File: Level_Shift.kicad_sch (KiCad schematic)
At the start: 22 parts, among them U23 74AVC4T245, U25 74AVC4T245, U26 74LVC8T245, U27 74LVC8T245

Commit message: Revision based on pre-production
-Added pull-down on the OE for the Digital output buffers
- increase board edge (was 0.3mm, but via and traces are 0.5mm away now)
- move power vias away from board edge
- Increase power via size from 0.6mm/0.3mm to 0.8mm/0.4mm in a couple of places
- Naming of level shifter output enable changed to make function clear throughout the design.
- Revised SMPS layout slightly to better use the space.
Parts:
- added R42, R43: 4.75k, Resistor_SMD:R_0402_1005Metric, symbol Device:R_Small_US
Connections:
- net GND: now also R42.1, R43.1
- net OE_Digital_Outputs_A: now also R43.2
- net OE_Digital_Outputs_B: now also R42.2
- net OE_Faults_0 renamed Cleaner_LevelShift_~{OE}_0
- net OE_Faults_1 renamed Cleaner_LevelShift_~{OE}_1
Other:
- moved on the sheet: R96, R97

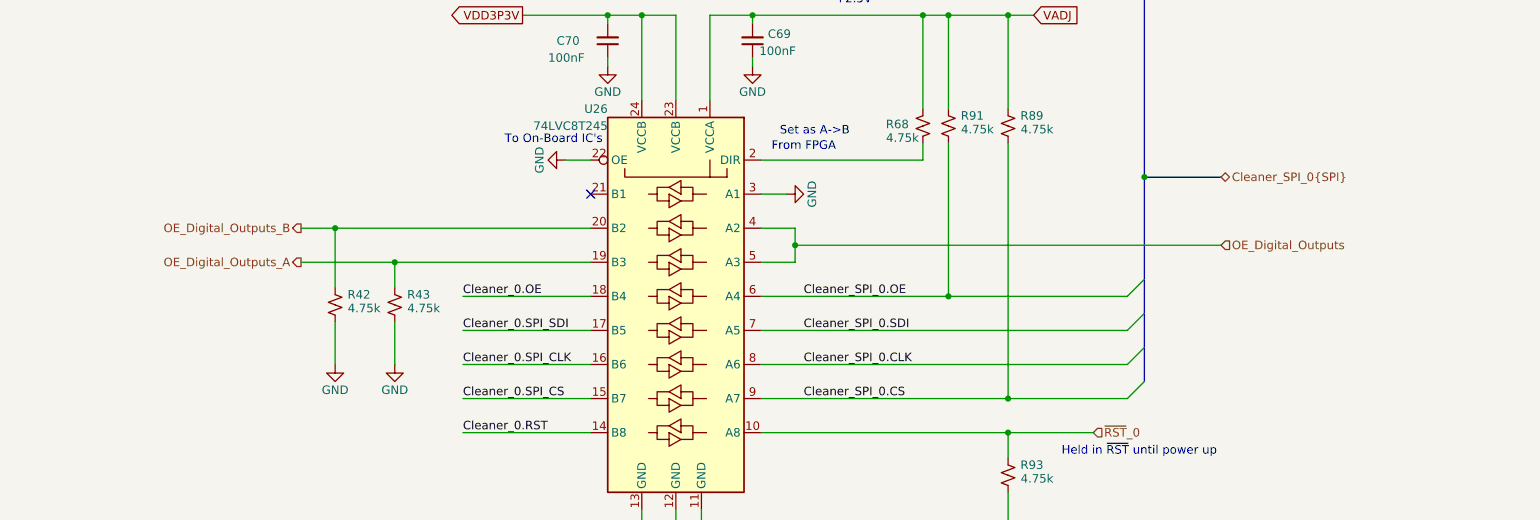
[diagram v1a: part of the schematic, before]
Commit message: Updates from Pre-production boards
- removed ground from mounting holes and added no-pop 0805 resistors to optionally ground the mounting holes.
- Adjusted placement of some test points.
- Made the test point loops non-populated parts, the pads will remain.
- Added silkscreen labels to the test points.
- Fixed pulldown resistor added in prevoius commit.
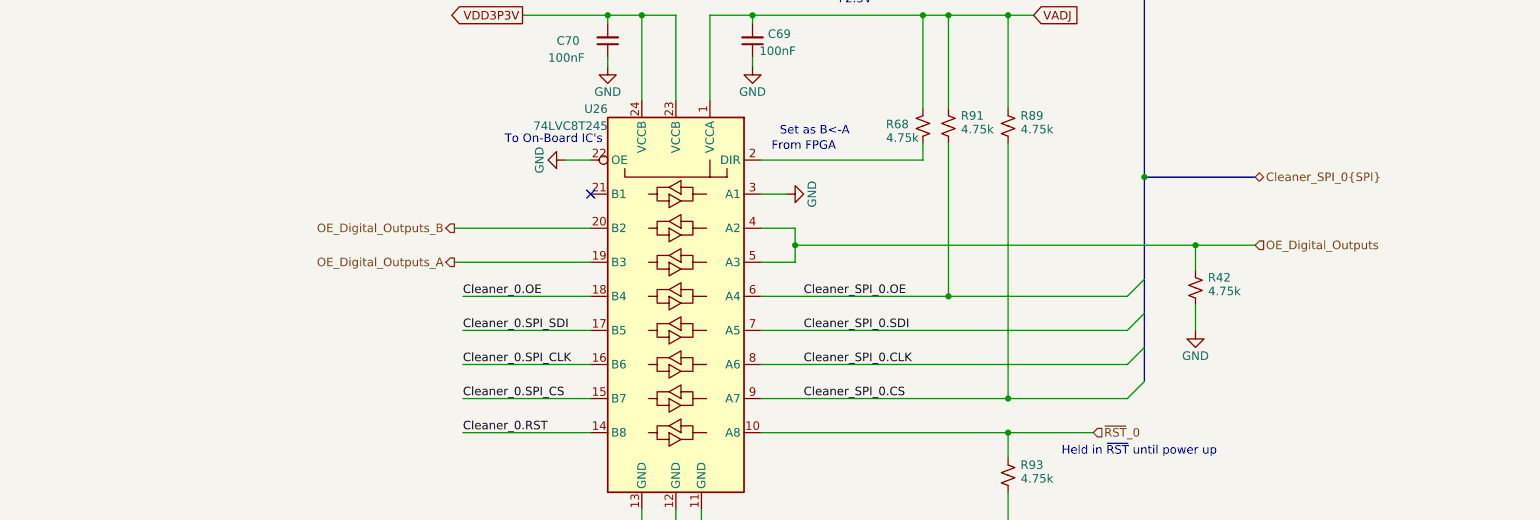
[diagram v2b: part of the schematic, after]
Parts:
- removed R43: 4.75k, Resistor_SMD:R_0402_1005Metric, symbol Device:R_Small_US
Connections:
- net OE_Digital_Outputs: now also R42.2
- net OE_Digital_Outputs_B: no longer R42.2
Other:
- note added: "Set as B<-A"
- moved on the sheet: R42
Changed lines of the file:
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@@
 		)
 	)
-	(text "Set as A->B"
+	(text "Set as B<-A"
 		(exclude_from_sim no)
 		(at 154.178 129.794 0)
@@
 	)
 	(junction
-		(at 77.47 143.51)
-		(diameter 0)
-		(color 0 0 0 0)
-	)
-	(junction
 		(at 297.18 99.06)
 		(diameter 0)
@@
 	)
 	(junction
+		(at 205.74 146.05)
+		(diameter 0)
+		(color 0 0 0 0)
+	)
+	(junction
 		(at 177.8 173.99)
 		(diameter 0)
@@
 	)
 	(junction
-		(at 86.36 148.59)
-		(diameter 0)
-		(color 0 0 0 0)
-	)
-	(junction
 		(at 363.22 134.62)
 		(diameter 0)
@@
 	(wire
 		(pts
-			(xy 86.36 148.59) (xy 86.36 152.4)
-		)
-		(stroke
-			(width 0)
-			(type default)
-		)
-	)
-	(wire
-		(pts
 			(xy 165.1 133.35) (xy 165.1 130.81)
 		)
@@
 	(bus
 		(pts
-			(xy 198.12 135.89) (xy 209.55 135.89)
+			(xy 198.12 135.89) (xy 214.63 135.89)
 		)
 		(stroke
@@
 	(wire
 		(pts
+			(xy 205.74 146.05) (xy 146.05 146.05)
+		)
+		(stroke
+			(width 0)
+			(type default)
+		)
+	)
+	(wire
+		(pts
 			(xy 355.6 38.1) (xy 355.6 48.26)
 		)
@@
 		)
 	)
-	(wire
-		(pts
-			(xy 77.47 143.51) (xy 77.47 152.4)
-		)
-		(stroke
-			(width 0)
-			(type default)
-		)
-	)
 	(bus
 		(pts
@@
 	(wire
 		(pts
-			(xy 86.36 148.59) (xy 115.57 148.59)
+			(xy 95.25 148.59) (xy 115.57 148.59)
 		)
 		(stroke
@@
 	(wire
 		(pts
-			(xy 72.39 143.51) (xy 77.47 143.51)
-		)
-		(stroke
-			(width 0)
-			(type default)
-		)
-	)
-	(wire
-		(pts
 			(xy 292.1 38.1) (xy 292.1 53.34)
 		)
@@
 	(wire
 		(pts
+			(xy 205.74 146.05) (xy 205.74 149.86)
+		)
+		(stroke
+			(width 0)
+			(type default)
+		)
+	)
+	(wire
+		(pts
 			(xy 288.29 110.49) (xy 288.29 123.19)
 		)
@@
 	(wire
 		(pts
-			(xy 77.47 143.51) (xy 115.57 143.51)
+			(xy 95.25 143.51) (xy 115.57 143.51)
 		)
 		(stroke
@@
 	(wire
 		(pts
-			(xy 72.39 148.59) (xy 86.36 148.59)
-		)
-		(stroke
-			(width 0)
-			(type default)
-		)
-	)
-	(wire
-		(pts
 			(xy 288.29 110.49) (xy 293.37 110.49)
 		)
@@
 	(wire
 		(pts
-			(xy 86.36 157.48) (xy 86.36 163.83)
+			(xy 205.74 154.94) (xy 205.74 158.75)
 		)
 		(stroke
@@
 	(wire
 		(pts
-			(xy 77.47 157.48) (xy 77.47 163.83)
-		)
-		(stroke
-			(width 0)
-			(type default)
-		)
-	)
-	(wire
-		(pts
 			(xy 119.38 39.37) (xy 119.38 40.64)
 		)
@@
 	(wire
 		(pts
-			(xy 209.55 146.05) (xy 146.05 146.05)
+			(xy 214.63 146.05) (xy 205.74 146.05)
 		)
 		(stroke
@@
 	(hierarchical_label "OE_Digital_Outputs"
 		(shape input)
-		(at 209.55 146.05 0)
+		(at 214.63 146.05 0)
 		(effects
 			(font
@@
 	(hierarchical_label "OE_Digital_Outputs_B"
 		(shape output)
-		(at 72.39 143.51 180)
+		(at 95.25 143.51 180)
 		(effects
 			(font
@@
 	(hierarchical_label "Cleaner_SPI_0{SPI}"
 		(shape bidirectional)
-		(at 209.55 135.89 0)
+		(at 214.63 135.89 0)
 		(effects
 			(font
@@
 	(hierarchical_label "OE_Digital_Outputs_A"
 		(shape output)
-		(at 72.39 148.59 180)
+		(at 95.25 148.59 180)
 		(effects
 			(font
@@
 	(symbol
 		(lib_id "power:GND")
-		(at 77.47 163.83 0)
+		(at 205.74 158.75 0)
 		(mirror y)
 		(unit 1)
@@
 		(dnp no)
 		(property "Reference" "#PWR0226"
-			(at 77.47 170.18 0)
+			(at 205.74 165.1 0)
 			(effects
 				(font
@@
 		)
 		(property "Value" "GND"
-			(at 77.47 167.64 0)
+			(at 205.74 162.56 0)
 			(effects
 				(font
@@
 		)
 		(property "Footprint" ""
-			(at 77.47 163.83 0)
+			(at 205.74 158.75 0)
 			(effects
 				(font
@@
 		)
 		(property "Datasheet" ""
-			(at 77.47 163.83 0)
+			(at 205.74 158.75 0)
 			(effects
 				(font
@@
 		)
 		(property "Description" ""
-			(at 77.47 163.83 0)
+			(at 205.74 158.75 0)
 			(effects
 				(font
@@
 	(symbol
 		(lib_id "Device:R_Small_US")
-		(at 77.47 154.94 180)
+		(at 205.74 152.4 180)
 		(unit 1)
 		(exclude_from_sim no)
@@
 		(dnp no)
 		(property "Reference" "R42"
-			(at 81.026 153.416 0)
+			(at 209.296 150.876 0)
 			(effects
 				(font
@@
 		)
 		(property "Value" "4.75k"
-			(at 81.788 155.448 0)
+			(at 210.058 152.908 0)
 			(effects
 				(font
@@
 		)
 		(property "Footprint" "Resistor_SMD:R_0402_1005Metric"
-			(at 77.47 154.94 0)
+			(at 205.74 152.4 0)
 			(effects
 				(font
@@
 		)
 		(property "Datasheet" "~"
-			(at 77.47 154.94 0)
+			(at 205.74 152.4 0)
 			(effects
 				(font
@@
 		)
 		(property "Description" "RES 4.75K OHM 1% 1/10W 0603"
-			(at 77.47 154.94 0)
+			(at 205.74 152.4 0)
 			(effects
 				(font
@@
 		)
 		(property "MPN" "RC0402FR-074K75L"
-			(at 77.47 154.94 90)
+			(at 205.74 152.4 90)
 			(effects
 				(font
@@
 		)
 		(property "Manufacturer" "Yageo"
-			(at 77.47 154.94 0)
+			(at 205.74 152.4 0)
 			(effects
 				(font
@@
 	)
 	(symbol
-		(lib_id "power:GND")
-		(at 86.36 163.83 0)
-		(mirror y)
-		(unit 1)
-		(exclude_from_sim no)
-		(in_bom yes)
-		(on_board yes)
-		(dnp no)
-		(property "Reference" "#PWR0227"
-			(at 86.36 170.18 0)
-			(effects
-				(font
-					(size 1.27 1.27)
-				)
-				(hide yes)
-			)
-		)
-		(property "Value" "GND"
-			(at 86.36 167.64 0)
-			(effects
-				(font
-					(size 1.27 1.27)
-				)
-			)
-		)
-		(property "Footprint" ""
-			(at 86.36 163.83 0)
-			(effects
-				(font
-					(size 1.27 1.27)
-				)
-				(hide yes)
-			)
-		)
-		(property "Datasheet" ""
-			(at 86.36 163.83 0)
-			(effects
-				(font
-					(size 1.27 1.27)
-				)
-				(hide yes)
-			)
-		)
-		(property "Description" ""
-			(at 86.36 163.83 0)
-			(effects
-				(font
-					(size 1.27 1.27)
-				)
-				(hide yes)
-			)
-		)
-		(pin "1"
-		)
-		(instances
-			(project "trigger-output-fmc"
-				(path "/1719e569-47c8-4fa0-8523-9c9686ef0dba/05ea2a42-fe0f-470f-b14d-98c7f1e9db32"
-					(reference "#PWR0227")
-					(unit 1)
-				)
-			)
-		)
-	)
-	(symbol
 		(lib_id "Device:R_Small_US")
 		(at 342.9 142.24 180)
@@
 					(unit 1)
 				)
-			)
-		)
-	)
-	(symbol
-		(lib_id "Device:R_Small_US")
-		(at 86.36 154.94 180)
-		(unit 1)
-		(exclude_from_sim no)
-		(in_bom yes)
-		(on_board yes)
-		(dnp no)
-		(property "Reference" "R43"
-			(at 89.916 153.416 0)
-			(effects
-				(font
-					(size 1.27 1.27)
-				)
-			)
-		)
-		(property "Value" "4.75k"
-			(at 90.678 155.448 0)
-			(effects
-				(font
-					(size 1.27 1.27)
-				)
-			)
-		)
-		(property "Footprint" "Resistor_SMD:R_0402_1005Metric"
-			(at 86.36 154.94 0)
-			(effects
-				(font
-					(size 1.27 1.27)
-				)
-				(hide yes)
-			)
-		)
-		(property "Datasheet" "~"
-			(at 86.36 154.94 0)
-			(effects
-				(font
-					(size 1.27 1.27)
-				)
-				(hide yes)
-			)
-		)
-		(property "Description" "RES 4.75K OHM 1% 1/10W 0603"
-			(at 86.36 154.94 0)
-			(effects
-				(font
-					(size 1.27 1.27)
-				)
-				(hide yes)
-			)
-		)
-		(property "MPN" "RC0402FR-074K75L"
-			(at 86.36 154.94 90)
-			(effects
-				(font
-					(size 1.27 1.27)
-				)
-				(hide yes)
-			)
-		)
-		(property "Manufacturer" "Yageo"
-			(at 86.36 154.94 0)
-			(effects
-				(font
-					(size 1.27 1.27)
-				)
-				(hide yes)
-			)
-		)
-		(pin "1"
-		)
-		(pin "2"
-		)
-		(instances
-			(project "trigger-output-fmc"
-				(path "/1719e569-47c8-4fa0-8523-9c9686ef0dba/05ea2a42-fe0f-470f-b14d-98c7f1e9db32"
-					(reference "R43")
-					(unit 1)
-				)

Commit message: Updated Version Number to 1.1
Updated Version Number to 1.1
-Added Test point for digital output LDO supply (TP10)
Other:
- title: FMC Template -> Trigger Output FMC
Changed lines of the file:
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@@
 	(paper "A3")
 	(title_block
-		(title "FMC Template")
-		(date "2026-01-26")
-		(rev "1.0")
+		(title "Trigger Output FMC")
+		(date "2026-10-06")
+		(rev "1.1")
 		(company "SPDX-FileCopyrightText: 2025 Osprey DCS")
 		(comment 1 "SPDX-License-Identifier: CERN-OHL-S-2.0+")
